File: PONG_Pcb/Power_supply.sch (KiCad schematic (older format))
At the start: 11 parts, among them J2 Input_Supply+5V, U2 LD1117S33TR_SOT223

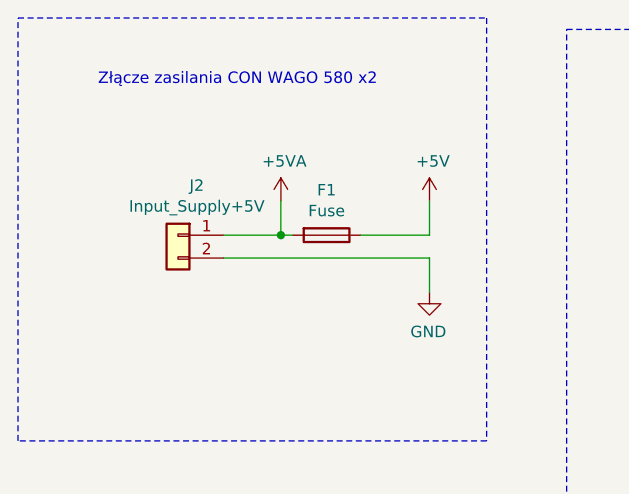
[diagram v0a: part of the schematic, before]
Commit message: Poprawki layoutu
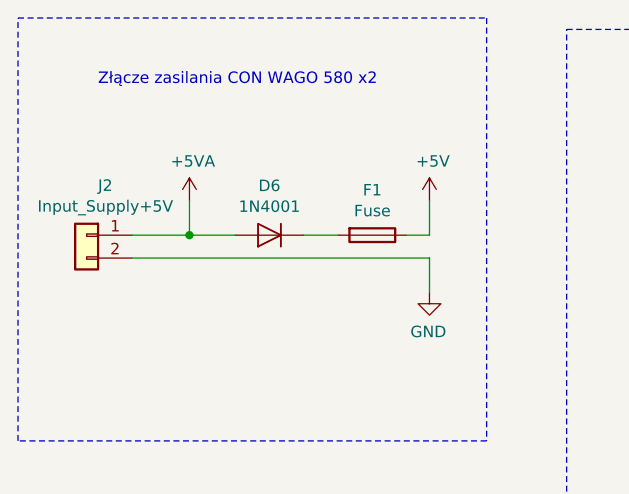
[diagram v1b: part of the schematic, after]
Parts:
- added D6: 1N4001, Diode_THT:D_DO-41_SOD81_P10.16mm_Horizontal, symbol Diode:1N4001
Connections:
- net +5VA: now also D6.2 (A); no longer F1.2
- new net: D6.1 (K), F1.2
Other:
- moved on the sheet: F1, J2
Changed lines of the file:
@@
 L Connector_Generic:Conn_01x02 J?
 U 1 1 5E83DA30
-P 1750 1750
+P 1350 1750
 AR Path="/5E80CCDD/5E83DA30" Ref="J?"  Part="1"
 AR Path="/5E80B14C/5E83DA30" Ref="J2"  Part="1"
 AR Path="/5E83DA30" Ref="J?"  Part="1"
-F 0 "J2" H 1668 1967 50  0000 C CNN
-F 1 "Input_Supply+5V" H 1668 1876 50  0000 C CNN
-F 2 "TerminalBlock_RND:TerminalBlock_RND_205-00001_1x02_P5.00mm_Horizontal" H 1750 1750 50  0001 C CNN
-F 3 "~" H 1750 1750 50  0001 C CNN
-	1    1750 1750
+F 0 "J2" H 1268 1967 50  0000 C CNN
+F 1 "Input_Supply+5V" H 1268 1876 50  0000 C CNN
+F 2 "TerminalBlock_RND:TerminalBlock_RND_205-00001_1x02_P5.00mm_Horizontal" H 1350 1750 50  0001 C CNN
+F 3 "~" H 1350 1750 50  0001 C CNN
+	1    1350 1750
 	-1   0    0    -1
 $EndComp
@@
 	2850 1850 2850 2000
 Wire Wire Line
-	2850 1850 1950 1850
+	2850 1850 1550 1850
 $Comp
 L Regulator_Linear:LD1117S33TR_SOT223 U2
@@
 L Device:Fuse F1
 U 1 1 5EA039B3
-P 2400 1750
-F 0 "F1" V 2203 1750 50  0000 C CNN
-F 1 "Fuse" V 2294 1750 50  0000 C CNN
-F 2 "Fuse:Fuse_Littelfuse_372_D8.50mm" V 2330 1750 50  0001 C CNN
-F 3 "~" H 2400 1750 50  0001 C CNN
-	1    2400 1750
+P 2600 1750
+F 0 "F1" V 2403 1750 50  0000 C CNN
+F 1 "Fuse" V 2494 1750 50  0000 C CNN
+F 2 "Fuse:Fuse_Littelfuse_372_D8.50mm" V 2530 1750 50  0001 C CNN
+F 3 "~" H 2600 1750 50  0001 C CNN
+	1    2600 1750
 	0    1    1    0
 $EndComp
-Wire Wire Line
-	2550 1750 2850 1750
-Wire Wire Line
-	2250 1750 2200 1750
 $Comp
 L power:+5V #PWR06
@@
 L power:+5VA #PWR0111
 U 1 1 5EA465DD
-P 2200 1600
-F 0 "#PWR0111" H 2200 1450 50  0001 C CNN
-F 1 "+5VA" H 2215 1773 50  0000 C CNN
-F 2 "" H 2200 1600 50  0001 C CNN
-F 3 "" H 2200 1600 50  0001 C CNN
-	1    2200 1600
-	1    0    0    -1
-$EndComp
-Wire Wire Line
-	2200 1600 2200 1750
-Connection ~ 2200 1750
-Wire Wire Line
-	2200 1750 1950 1750
+P 1800 1600
+F 0 "#PWR0111" H 1800 1450 50  0001 C CNN
+F 1 "+5VA" H 1815 1773 50  0000 C CNN
+F 2 "" H 1800 1600 50  0001 C CNN
+F 3 "" H 1800 1600 50  0001 C CNN
+	1    1800 1600
+	1    0    0    -1
+$EndComp
+Wire Wire Line
+	1800 1600 1800 1750
+Connection ~ 1800 1750
+Wire Wire Line
+	1800 1750 1550 1750
+$Comp
+L Diode:1N4001 D6
+U 1 1 5EC3FFE2
+P 2150 1750
+F 0 "D6" H 2150 1534 50  0000 C CNN
+F 1 "1N4001" H 2150 1625 50  0000 C CNN
+F 2 "Diode_THT:D_DO-41_SOD81_P10.16mm_Horizontal" H 2150 1575 50  0001 C CNN
+F 3 "http://www.vishay.com/docs/88503/1n4001.pdf" H 2150 1750 50  0001 C CNN
+	1    2150 1750
+	-1   0    0    1
+$EndComp
+Wire Wire Line
+	1800 1750 2000 1750
+Wire Wire Line
+	2300 1750 2450 1750
+Wire Wire Line
+	2750 1750 2850 1750
 $EndSCHEMATC

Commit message: Ostatnia wersja
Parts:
- D6: footprint Diode_THT:D_DO-41_SOD81_P10.16mm_Horizontal -> Diode_SMD:D_SMC-RM10_Universal_Handsoldering
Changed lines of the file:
@@
 Connection ~ 7300 1650
-Wire Wire Line
-	7300 1650 7700 1650
 Wire Wire Line
 	7700 1650 7700 1750
@@
 	8800 1650 8800 1750
 Connection ~ 8800 1650
-Wire Wire Line
-	8800 1650 9200 1650
 Wire Wire Line
 	9200 1650 9200 1750
@@
 F 0 "D6" H 2150 1534 50  0000 C CNN
 F 1 "1N4001" H 2150 1625 50  0000 C CNN
-F 2 "Diode_THT:D_DO-41_SOD81_P10.16mm_Horizontal" H 2150 1575 50  0001 C CNN
+F 2 "Diode_SMD:D_SMC-RM10_Universal_Handsoldering" H 2150 1575 50  0001 C CNN
 F 3 "http://www.vishay.com/docs/88503/1n4001.pdf" H 2150 1750 50  0001 C CNN
 	1    2150 1750
@@
 Wire Wire Line
 	2750 1750 2850 1750
+Wire Wire Line
+	7300 1650 7700 1650
+Wire Wire Line
+	8800 1650 9200 1650
 $EndSCHEMATC

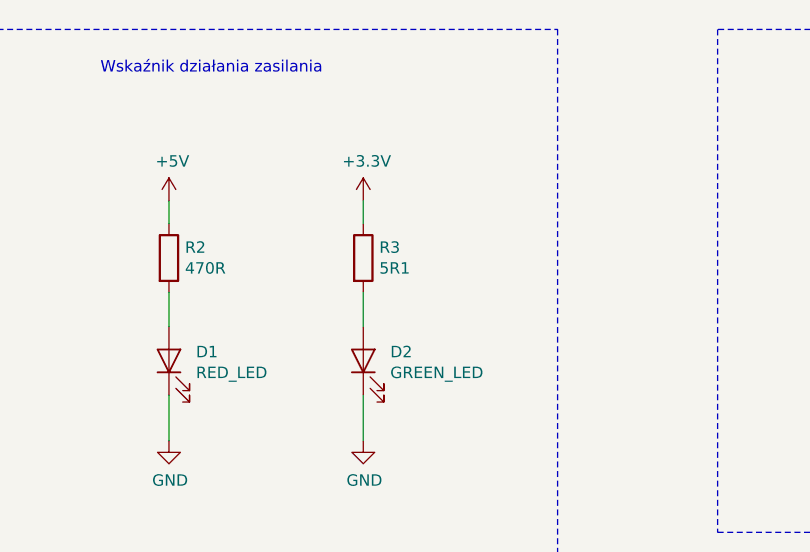
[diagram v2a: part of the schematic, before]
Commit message: Drobna zmiana wartości elementów
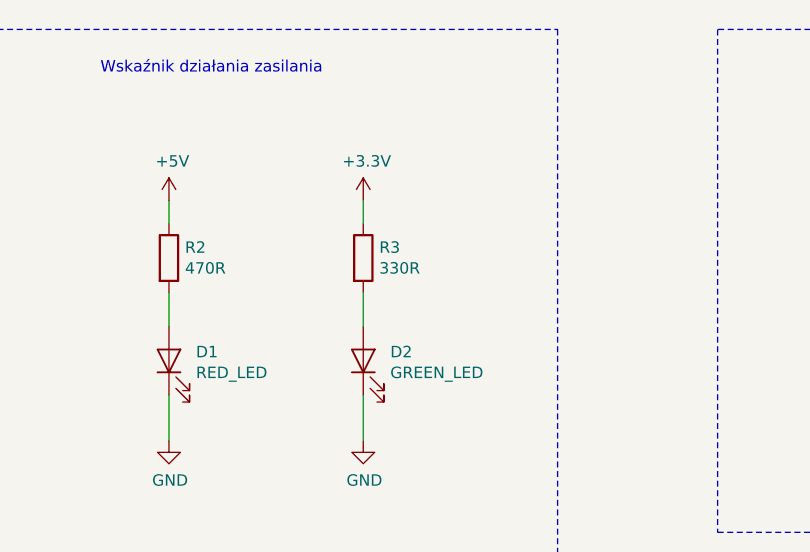
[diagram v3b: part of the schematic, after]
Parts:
- R3: value 5R1 -> 330R
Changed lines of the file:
@@
 P 5050 1850
 F 0 "R3" H 5120 1896 50  0000 L CNN
-F 1 "5R1" H 5120 1805 50  0000 L CNN
+F 1 "330R" H 5120 1805 50  0000 L CNN
 F 2 "Resistor_SMD:R_0603_1608Metric_Pad1.05x0.95mm_HandSolder" V 4980 1850 50  0001 C CNN
 F 3 "~" H 5050 1850 50  0001 C CNN

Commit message: poprawki koncowe
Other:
- moved on the sheet: C2, C3, C4, C5, D1, D2, D6, F1, J2, R2, R3, U2
